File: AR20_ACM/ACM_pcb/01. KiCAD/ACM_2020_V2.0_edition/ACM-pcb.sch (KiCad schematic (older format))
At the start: 32 parts, among them IC1 MCP25625T-E_ML, J1 TC2030-MCP-NL, P1 Conn_02x15_Odd_Even, Q1 Q_PMOS_DGS, U1 ATmega328P-AU, U3 NCV890430MW50TXG, Y1 16.0Mhz

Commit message: Simon adjustment 1 of 2
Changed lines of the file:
@@
 EESchema Schematic File Version 4
-EELAYER 30 0
+LIBS:ACM-pcb-cache
+EELAYER 29 0
 EELAYER END
 $Descr A4 11693 8268
@@
 P 8550 4200
 F 0 "IC1" H 9894 3896 50  0000 L CNN
-F 1 "MCP25625T-E_ML" H 9894 3805 50  0000 L CNN
+F 1 "MCP25625T-E_ML" H 9900 2900 50  0000 L CNN
 F 2 "QFN65P600X600X100-29N-D" H 9700 4700 50  0001 L CNN
 F 3 "https://www.mouser.com/datasheet/2/268/20005282B-708896.pdf" H 9700 4600 50  0001 L CNN

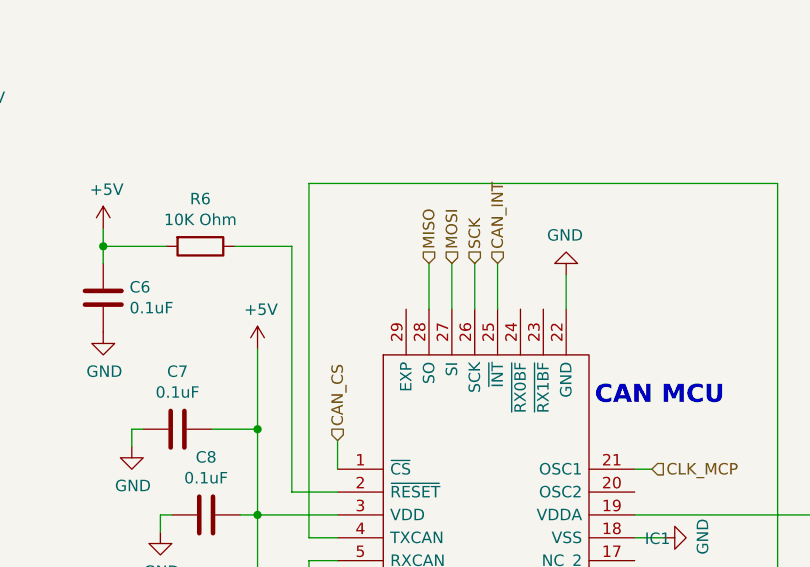
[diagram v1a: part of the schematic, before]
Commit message: Checked MCP25625 and adjusted traces.
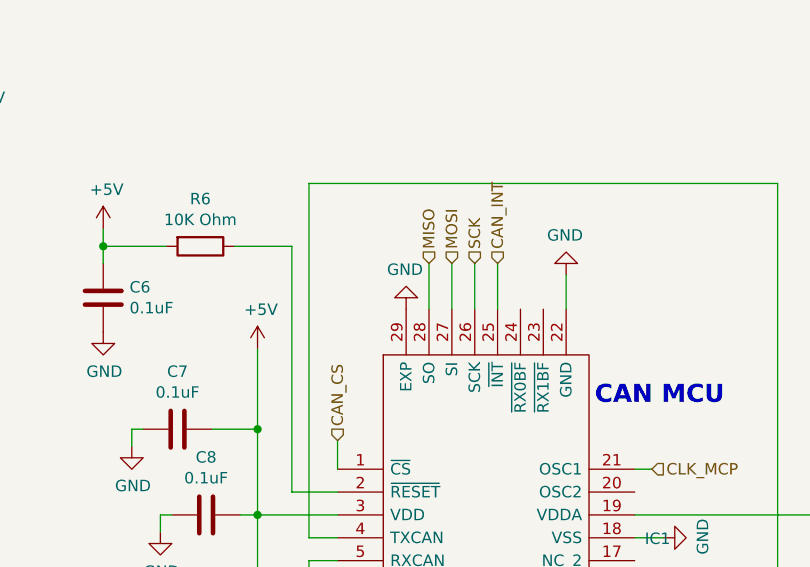
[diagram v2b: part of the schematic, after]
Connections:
- net GND: now also IC1.29 (EXP)
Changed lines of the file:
@@
 Text HLabel 9925 4200 2    50   Input ~ 0
 CLK_MCP
+$Comp
+L ACM-pcb-rescue:GND-power-ACM_Y2020V0.1-rescue #PWR0107
+U 1 1 5E6D5221
+P 8850 3500
+F 0 "#PWR0107" H 8850 3250 50  0001 C CNN
+F 1 "GND" H 8855 3327 50  0000 C CNN
+F 2 "" H 8850 3500 50  0001 C CNN
+F 3 "" H 8850 3500 50  0001 C CNN
+	1    8850 3500
+	-1   0    0    1
+$EndComp
 $EndSCHEMATC

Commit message: Circuit protecion fixed
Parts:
- removed D2: 2.4V, Diode_SMD:D_SOD-523, symbol ACM-pcb-rescue:D_Zener-Device-ACM_Y2020V0.1-rescue
- removed Q1: Q_PMOS_DGS, Package_TO_SOT_SMD:SOT-23, symbol ACM-pcb-rescue:Q_PMOS_GSD-Device-ACM_Y2020V0.1-rescue
- added D4: D_Schottky_MBR0520LT1G, ACM_2020_V2:D_schotky_MBR0520LT1G, symbol ACM-pcb-rescue:D_Schottky_MBR0520LT1G
- added Q1: Q_PMOS_DMP3099L-13, ACM_2020_V2:Pmos_DMP3099L-13, symbol ACM-pcb-rescue:Q_PMOS_DMP3099L-13
- IC1: footprint QFN65P600X600X100-29N-D -> ACM_2020_V2:QFN65P600X600X100-29N-D
- R2: value 100K Ohm -> 10K Ohm; Farnell https://no.farnell.com/vishay/crcw0402100kfked/res-100k-1-0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 -> (none)
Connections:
- net +12V: now also D4.2 (A); no longer F1.2
- net +12V_Safe: now also D1.1 (K), F1.1, R2.2, Q1.1 (G)
- net +5V: now also Q1.2 (S); no longer J1.2 (5V)
- net GND: now also R2.1; no longer R2.2
- new net: J1.2 (5V), Q1.3 (D)
- new net: D4.1 (K), F1.2
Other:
- note removed: "NB! Vgs max: ±10V!\n2.4V zener diode\nfor Vgs -2.4V"
- note removed: "P-mosfet for reverse\npolarity protection"
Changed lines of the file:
@@
 EESchema Schematic File Version 4
-LIBS:ACM-pcb-cache
-EELAYER 29 0
+EELAYER 30 0
 EELAYER END
 $Descr A4 11693 8268
@@
 Wire Wire Line
 	3600 5350 3500 5350
-Text Notes 4925 3350 0    79   ~ 16
+Text Notes 4575 2925 0    79   ~ 16
 Power and protection circuits
 Text Notes 1925 3850 0    79   ~ 16
@@
 L ACM-pcb-rescue:+12V-power-ACM_Y2020V0.1-rescue #PWR017
 U 1 1 5D442037
-P 5800 3675
-F 0 "#PWR017" H 5800 3525 50  0001 C CNN
-F 1 "+12V" H 5815 3848 50  0000 C CNN
-F 2 "" H 5800 3675 50  0001 C CNN
-F 3 "" H 5800 3675 50  0001 C CNN
-	1    5800 3675
+P 5800 3375
+F 0 "#PWR017" H 5800 3225 50  0001 C CNN
+F 1 "+12V" H 5815 3548 50  0000 C CNN
+F 2 "" H 5800 3375 50  0001 C CNN
+F 3 "" H 5800 3375 50  0001 C CNN
+	1    5800 3375
 	1    0    0    -1
 $EndComp
@@
 Wire Wire Line
 	5275 4150 5275 4225
-$Comp
-L ACM-pcb-rescue:GND-power-ACM_Y2020V0.1-rescue #PWR016
-U 1 1 5D3F2B57
-P 5500 5250
-F 0 "#PWR016" H 5500 5000 50  0001 C CNN
-F 1 "GND" H 5505 5077 50  0000 C CNN
-F 2 "" H 5500 5250 50  0001 C CNN
-F 3 "" H 5500 5250 50  0001 C CNN
-	1    5500 5250
-	1    0    0    -1
-$EndComp
 Text Notes 4775 4125 0    39   ~ 0
 Zener diode for\novervoltage protection
-Text Notes 4900 4675 0    39   ~ 0
-P-mosfet for reverse\npolarity protection
 Text Notes 5875 3900 0    39   ~ 0
 Polyfuse for\novercurrent protection
@@
 	0    -1   -1   0
 $EndComp
-$Comp
-L ACM-pcb-rescue:Q_PMOS_GSD-Device-ACM_Y2020V0.1-rescue Q1
-U 1 1 5D49C78B
-P 5700 4650
-F 0 "Q1" H 5906 4696 50  0000 L CNN
-F 1 "Q_PMOS_DGS" H 5906 4605 50  0000 L CNN
-F 2 "Package_TO_SOT_SMD:SOT-23" H 5900 4750 50  0001 C CNN
-F 3 "http://www.farnell.com/datasheets/2040104.pdf?_ga=2.59461290.620744209.1564174328-1415930916.1560114588&_gac=1.194072415.1564075292.CjwKCAjwpuXpBRAAEiwAyRRPgXwHZ1wF4xXBoNI_FJEvoVORJn7NbJB9jjbidsg8_qDnlLi_44u6wRoCV2MQAvD_BwE" H 5700 4650 50  0001 C CNN
-F 4 "2543551" H 5700 4650 50  0001 C CNN "Farnell"
-	1    5700 4650
-	1    0    0    -1
-$EndComp
-Wire Wire Line
-	5800 4850 5800 4950
 Text Notes 950  4075 0    50   ~ 0
 Trenger flere Decupling Caps?
-Text Notes 5475 4925 2    50   ~ 0
-NB! Vgs max: ±10V!\n2.4V zener diode\nfor Vgs -2.4V
-$Comp
-L ACM-pcb-rescue:R-Device-ACM_Y2020V0.1-rescue R2
-U 1 1 5D4B82FB
-P 5500 5100
-F 0 "R2" H 5570 5146 50  0000 L CNN
-F 1 "100K Ohm" H 5570 5055 50  0000 L CNN
-F 2 "Resistor_SMD:R_0402_1005Metric" V 5430 5100 50  0001 C CNN
-F 3 "http://www.farnell.com/datasheets/2310790.pdf?_ga=2.261974922.620744209.1564174328-1415930916.1560114588&_gac=1.24838472.1564075292.CjwKCAjwpuXpBRAAEiwAyRRPgXwHZ1wF4xXBoNI_FJEvoVORJn7NbJB9jjbidsg8_qDnlLi_44u6wRoCV2MQAvD_BwE" H 5500 5100 50  0001 C CNN
-F 4 "https://no.farnell.com/vishay/crcw0402100kfked/res-100k-1-0-063w-0402-thick-film/dp/1469671" H 5500 5100 50  0001 C CNN "Farnell"
-	1    5500 5100
-	1    0    0    -1
-$EndComp
-$Comp
-L ACM-pcb-rescue:D_Zener-Device-ACM_Y2020V0.1-rescue D2
-U 1 1 5D4B9259
-P 5650 4950
-F 0 "D2" H 5650 4734 50  0000 C CNN
-F 1 "2.4V" H 5650 4825 50  0000 C CNN
-F 2 "Diode_SMD:D_SOD-523" H 5650 4950 50  0001 C CNN
-F 3 "http://www.farnell.com/datasheets/2174102.pdf?_ga=2.89435932.620744209.1564174328-1415930916.1560114588&_gac=1.184758107.1564075292.CjwKCAjwpuXpBRAAEiwAyRRPgXwHZ1wF4xXBoNI_FJEvoVORJn7NbJB9jjbidsg8_qDnlLi_44u6wRoCV2MQAvD_BwE" H 5650 4950 50  0001 C CNN
-F 4 "https://no.farnell.com/nexperia/bzx585-c2v4-115/diode-zener-0-3w-2-4v-sod523/dp/1907635" H 5650 4950 50  0001 C CNN "Farnell"
-	1    5650 4950
-	-1   0    0    1
-$EndComp
-Wire Wire Line
-	5500 4650 5500 4950
-Connection ~ 5500 4950
 Wire Wire Line
 	5800 3675 5800 3750
-Wire Wire Line
-	5800 3950 5800 4150
 Wire Wire Line
 	5675 4150 5800 4150
 Connection ~ 5800 4150
-Wire Wire Line
-	5800 4150 5800 4450
 Wire Wire Line
 	6600 1975 6725 1975
@@
 	0    -1   -1   0
 $EndComp
-Wire Wire Line
-	5800 4950 6125 4950
-Connection ~ 5800 4950
-Text GLabel 6125 4950 2    50   Input ~ 0
-+12V_Safe
 Text GLabel 4625 5725 1    50   Input ~ 0
 +12V_Safe
@@
 Wire Wire Line
 	2975 1325 3075 1325
-Wire Wire Line
-	3075 1125 3075 1050
-Wire Wire Line
-	2975 1125 3075 1125
 Text Notes 1850 700  0    79   ~ 16
 ICSP
@@
 L ACM-pcb-rescue:+5V-power-ACM_Y2020V0.1-rescue #PWR07
 U 1 1 5D3A42C5
-P 3075 1050
-F 0 "#PWR07" H 3075 900 50  0001 C CNN
-F 1 "+5V" H 3090 1223 50  0000 C CNN
-F 2 "" H 3075 1050 50  0001 C CNN
-F 3 "" H 3075 1050 50  0001 C CNN
-	1    3075 1050
-	1    0    0    -1
+P 4125 1125
+F 0 "#PWR07" H 4125 975 50  0001 C CNN
+F 1 "+5V" H 4140 1298 50  0000 C CNN
+F 2 "" H 4125 1125 50  0001 C CNN
+F 3 "" H 4125 1125 50  0001 C CNN
+	1    4125 1125
+	0    1    1    0
 $EndComp
 $Comp
@@
 F 0 "IC1" H 9894 3896 50  0000 L CNN
 F 1 "MCP25625T-E_ML" H 9900 2900 50  0000 L CNN
-F 2 "QFN65P600X600X100-29N-D" H 9700 4700 50  0001 L CNN
+F 2 "ACM_2020_V2:QFN65P600X600X100-29N-D" H 9700 4700 50  0001 L CNN
 F 3 "https://www.mouser.com/datasheet/2/268/20005282B-708896.pdf" H 9700 4600 50  0001 L CNN
 F 4 "Microchip Technology MCP25625T-E/ML, CAN Controller 1Mbit/s CAN 2.0B, 28-Pin QFN" H 9700 4500 50  0001 L CNN "Description"
@@
 	-1   0    0    1
 $EndComp
+$Comp
+L ACM-pcb-rescue:Q_PMOS_DMP3099L-13 Q1
+U 1 1 5F70E300
+P 3925 1225
+F 0 "Q1" V 4268 1225 50  0000 C CNN
+F 1 "Q_PMOS_DMP3099L-13" V 4177 1225 50  0000 C CNN
+F 2 "ACM_2020_V2:Pmos_DMP3099L-13" H 4125 1325 50  0001 C CNN
+F 3 "" H 3925 1225 50  0001 C CNN
+	1    3925 1225
+	0    -1   -1   0
+$EndComp
+$Comp
+L ACM-pcb-rescue:D_Schottky_MBR0520LT1G D4
+U 1 1 5F71C208
+P 5800 3525
+F 0 "D4" H 5800 3742 50  0000 C CNN
+F 1 "D_Schottky_MBR0520LT1G" H 5800 3651 50  0000 C CNN
+F 2 "ACM_2020_V2:D_schotky_MBR0520LT1G" H 5800 3525 50  0001 C CNN
+F 3 "~" H 5800 3525 50  0001 C CNN
+	1    5800 3525
+	0    -1   -1   0
+$EndComp
+Wire Wire Line
+	5800 3950 5800 4150
+Text GLabel 5800 4525 3    50   Input ~ 0
++12V_Safe
+Wire Wire Line
+	5800 4150 5800 4525
+Text GLabel 3925 1750 3    50   Input ~ 0
++12V_Safe
+$Comp
+L ACM-pcb-rescue:R-Device-ACM_Y2020V0.1-rescue R2
+U 1 1 5F78E3CB
+P 4075 1550
+F 0 "R2" V 3868 1550 50  0000 C CNN
+F 1 "10K Ohm" V 3959 1550 50  0000 C CNN
+F 2 "Resistor_SMD:R_0402_1005Metric" V 4005 1550 50  0001 C CNN
+F 3 "~" H 4075 1550 50  0001 C CNN
+	1    4075 1550
+	0    1    1    0
+$EndComp
+$Comp
+L ACM-pcb-rescue:GND-power-ACM_Y2020V0.1-rescue #PWR0110
+U 1 1 5F7936AE
+P 4225 1550
+F 0 "#PWR0110" H 4225 1300 50  0001 C CNN
+F 1 "GND" H 4230 1377 50  0000 C CNN
+F 2 "" H 4225 1550 50  0001 C CNN
+F 3 "" H 4225 1550 50  0001 C CNN
+	1    4225 1550
+	0    -1   -1   0
+$EndComp
+Wire Wire Line
+	3925 1425 3925 1550
+Connection ~ 3925 1550
+Wire Wire Line
+	3925 1550 3925 1750
+Wire Wire Line
+	2975 1125 3725 1125
 $EndSCHEMATC

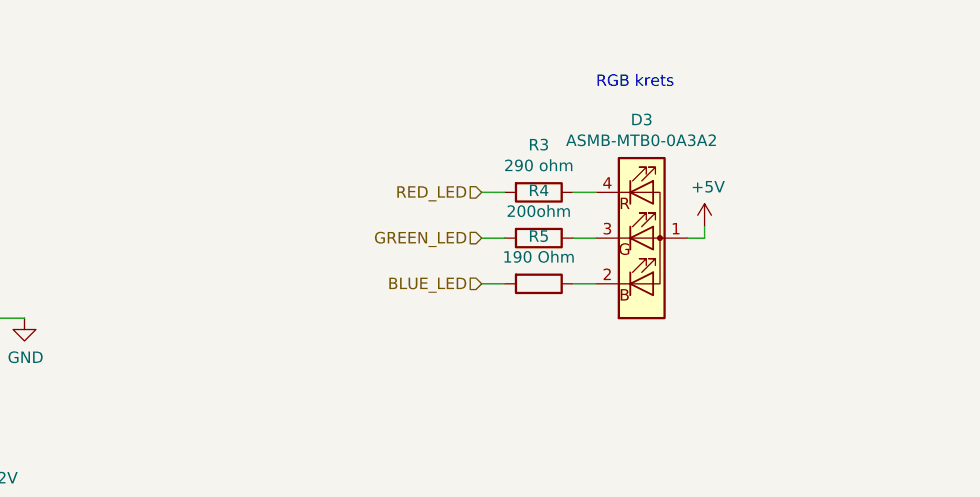
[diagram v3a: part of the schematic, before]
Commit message: Changed RGB light
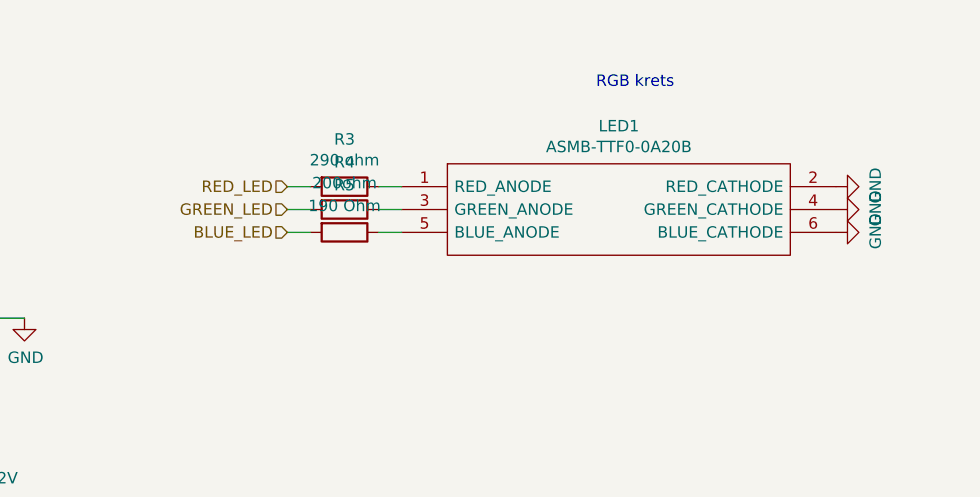
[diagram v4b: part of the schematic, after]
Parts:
- removed D3: ASMB-MTB0-0A3A2, LED_SMD:LED_Avago_PLCC4_3.2x2.8mm_CW, symbol ACM-pcb-rescue:ASMB-MTB0-0A3A2-LED-ACM_Y2020V0.1-rescue
- added LED1: ASMB-TTF0-0A20B, ASMB-TTF0-0A20B:ASMBTTF00A20B, symbol ASMB-TTF0-0A20B:ASMB-TTF0-0A20B
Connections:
- net GND: now also LED1.2 (RED_CATHODE), LED1.4 (GREEN_CATHODE), LED1.6 (BLUE_CATHODE)
- net at R5.1: now also LED1.5 (BLUE_ANODE)
- net at R4.1: now also LED1.3 (GREEN_ANODE)
- net at R3.1: now also LED1.1 (RED_ANODE)
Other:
- moved on the sheet: R3, R4, R5
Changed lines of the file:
@@
-$EndComp
-$Comp
-L ACM-pcb-rescue:ASMB-MTB0-0A3A2-LED-ACM_Y2020V0.1-rescue D3
-U 1 1 5DD7E33E
-P 9825 1525
-F 0 "D3" H 9825 2042 50  0000 C CNN
-F 1 "ASMB-MTB0-0A3A2" H 9825 1951 50  0000 C CNN
-F 2 "LED_SMD:LED_Avago_PLCC4_3.2x2.8mm_CW" H 9825 2025 50  0001 C CNN
-F 3 "https://docs.broadcom.com/docs/AV02-4186EN" H 9825 1075 50  0001 C CNN
-	1    9825 1525
-	1    0    0    -1
 $EndComp
 $Comp
 L ACM-pcb-rescue:R-Device-ACM_Y2020V0.1-rescue R3
 U 1 1 5DD8F0AE
-P 9375 1325
-F 0 "R3" V 9168 1325 50  0000 C CNN
-F 1 "290 ohm" V 9259 1325 50  0000 C CNN
-F 2 "Resistor_SMD:R_0402_1005Metric" V 9305 1325 50  0001 C CNN
-F 3 "~" H 9375 1325 50  0001 C CNN
-	1    9375 1325
+P 8525 1300
+F 0 "R3" V 8318 1300 50  0000 C CNN
+F 1 "290 ohm" V 8409 1300 50  0000 C CNN
+F 2 "Resistor_SMD:R_0402_1005Metric" V 8455 1300 50  0001 C CNN
+F 3 "~" H 8525 1300 50  0001 C CNN
+	1    8525 1300
 	0    1    1    0
 $EndComp
@@
 L ACM-pcb-rescue:R-Device-ACM_Y2020V0.1-rescue R4
 U 1 1 5DD96084
-P 9375 1525
-F 0 "R4" V 9168 1525 50  0000 C CNN
-F 1 "200ohm" V 9259 1525 50  0000 C CNN
-F 2 "Resistor_SMD:R_0402_1005Metric" V 9305 1525 50  0001 C CNN
-F 3 "~" H 9375 1525 50  0001 C CNN
-	1    9375 1525
+P 8525 1400
+F 0 "R4" V 8318 1400 50  0000 C CNN
+F 1 "200ohm" V 8409 1400 50  0000 C CNN
+F 2 "Resistor_SMD:R_0402_1005Metric" V 8455 1400 50  0001 C CNN
+F 3 "~" H 8525 1400 50  0001 C CNN
+	1    8525 1400
 	0    1    1    0
 $EndComp
@@
 L ACM-pcb-rescue:R-Device-ACM_Y2020V0.1-rescue R5
 U 1 1 5DD9CFD2
-P 9375 1725
-F 0 "R5" V 9168 1725 50  0000 C CNN
-F 1 "190 Ohm" V 9259 1725 50  0000 C CNN
-F 2 "Resistor_SMD:R_0402_1005Metric" V 9305 1725 50  0001 C CNN
-F 3 "~" H 9375 1725 50  0001 C CNN
-	1    9375 1725
-	0    1    1    0
-$EndComp
-Wire Wire Line
-	9625 1325 9525 1325
-Wire Wire Line
-	9625 1525 9525 1525
-Wire Wire Line
-	9625 1725 9525 1725
-$Comp
-L ACM-pcb-rescue:+5V-power-ACM_Y2020V0.1-rescue #PWR0103
-U 1 1 5DDBB889
-P 10100 1475
-F 0 "#PWR0103" H 10100 1325 50  0001 C CNN
-F 1 "+5V" H 10115 1648 50  0000 C CNN
-F 2 "" H 10100 1475 50  0001 C CNN
-F 3 "" H 10100 1475 50  0001 C CNN
-	1    10100 1475
-	1    0    0    -1
-$EndComp
-Wire Wire Line
-	10100 1475 10100 1525
-Wire Wire Line
-	10100 1525 10025 1525
-Text HLabel 9125 1725 0    50   Input ~ 0
+P 8525 1500
+F 0 "R5" V 8318 1500 50  0000 C CNN
+F 1 "190 Ohm" V 8409 1500 50  0000 C CNN
+F 2 "Resistor_SMD:R_0402_1005Metric" V 8455 1500 50  0001 C CNN
+F 3 "~" H 8525 1500 50  0001 C CNN
+	1    8525 1500
+	0    1    1    0
+$EndComp
+Wire Wire Line
+	8775 1300 8675 1300
+Wire Wire Line
+	8775 1400 8675 1400
+Wire Wire Line
+	8775 1500 8675 1500
+Text HLabel 8275 1500 0    50   Input ~ 0
 BLUE_LED
-Text HLabel 9125 1325 0    50   Input ~ 0
+Text HLabel 8275 1300 0    50   Input ~ 0
 RED_LED
-Text HLabel 9125 1525 0    50   Input ~ 0
+Text HLabel 8275 1400 0    50   Input ~ 0
 GREEN_LED
 Wire Wire Line
-	9125 1325 9225 1325
-Wire Wire Line
-	9225 1525 9125 1525
-Wire Wire Line
-	9225 1725 9125 1725
+	8275 1300 8375 1300
+Wire Wire Line
+	8375 1400 8275 1400
+Wire Wire Line
+	8375 1500 8275 1500
 Text Notes 9625 875  0    50   ~ 0
 RGB krets\n
@@
 Wire Wire Line
 	2975 1125 3725 1125
+$Comp
+L ASMB-TTF0-0A20B:ASMB-TTF0-0A20B LED1
+U 1 1 5F81B4A2
+P 8775 1300
+F 0 "LED1" H 9725 1565 50  0000 C CNN
+F 1 "ASMB-TTF0-0A20B" H 9725 1474 50  0000 C CNN
+F 2 "ASMB-TTF0-0A20B:ASMBTTF00A20B" H 10525 1400 50  0001 L CNN
+F 3 "https://componentsearchengine.com/Datasheets/1/ASMB-TTF0-0A20B.pdf" H 10525 1300 50  0001 L CNN
+F 4 "BROADCOM LIMITED - ASMB-TTF0-0A20B - LED, RGB, 710/1840/410MCD, PLCC-6" H 10525 1200 50  0001 L CNN "Description"
+F 5 "2" H 10525 1100 50  0001 L CNN "Height"
+F 6 "Avago Technologies" H 10525 1000 50  0001 L CNN "Manufacturer_Name"
+F 7 "ASMB-TTF0-0A20B" H 10525 900 50  0001 L CNN "Manufacturer_Part_Number"
+F 8 "ASMB-TTF0-0A20B" H 10525 800 50  0001 L CNN "Arrow Part Number"
+F 9 "" H 10525 700 50  0001 L CNN "Arrow Price/Stock"
+F 10 "630-ASMB-TTF0-0A20B" H 10525 600 50  0001 L CNN "Mouser Part Number"
+F 11 "https://www.mouser.co.uk/ProductDetail/Broadcom-Avago/ASMB-TTF0-0A20B?qs=j%252B1pi9TdxUbzVLPA%2F5LflQ%3D%3D" H 10525 500 50  0001 L CNN "Mouser Price/Stock"
+	1    8775 1300
+	1    0    0    -1
+$EndComp
+$Comp
+L ACM-pcb-rescue:GND-power-ACM_Y2020V0.1-rescue #PWR0103
+U 1 1 5F82C62E
+P 10675 1300
+F 0 "#PWR0103" H 10675 1050 50  0001 C CNN
+F 1 "GND" H 10680 1127 50  0000 C CNN
+F 2 "" H 10675 1300 50  0001 C CNN
+F 3 "" H 10675 1300 50  0001 C CNN
+	1    10675 1300
+	0    -1   -1   0
+$EndComp
+$Comp
+L ACM-pcb-rescue:GND-power-ACM_Y2020V0.1-rescue #PWR0111
+U 1 1 5F8309A5
+P 10675 1400
+F 0 "#PWR0111" H 10675 1150 50  0001 C CNN
+F 1 "GND" H 10680 1227 50  0000 C CNN
+F 2 "" H 10675 1400 50  0001 C CNN
+F 3 "" H 10675 1400 50  0001 C CNN
+	1    10675 1400
+	0    -1   -1   0
+$EndComp
+$Comp
+L ACM-pcb-rescue:GND-power-ACM_Y2020V0.1-rescue #PWR0112
+U 1 1 5F834774
+P 10675 1500
+F 0 "#PWR0112" H 10675 1250 50  0001 C CNN
+F 1 "GND" H 10680 1327 50  0000 C CNN
+F 2 "" H 10675 1500 50  0001 C CNN
+F 3 "" H 10675 1500 50  0001 C CNN
+	1    10675 1500
+	0    -1   -1   0
+$EndComp
 $EndSCHEMATC
